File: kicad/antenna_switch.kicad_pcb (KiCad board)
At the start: 2 copper layers, 213.3 x 96 mm, 153 parts, among them J1 Conn_02x07_Odd_Even, J2 Conn_01x02, K1 Fujitsu_FTR-K1C, K10 Fujitsu_FTR-K1C, K11 Fujitsu_FTR-K1C, K12 Fujitsu_FTR-K1C, K13 Fujitsu_FTR-K1C, K14 Fujitsu_FTR-K1C, K15 Fujitsu_FTR-K1C, K16 Fujitsu_FTR-K1C, K17 Fujitsu_FTR-K1C, K18 Fujitsu_FTR-K1C, K2 Fujitsu_FTR-K1C, K3 Fujitsu_FTR-K1C, K4 Fujitsu_FTR-K1C, K5 Fujitsu_FTR-K1C, K6 Fujitsu_FTR-K1C, K7 Fujitsu_FTR-K1C, K8 Fujitsu_FTR-K1C, K9 Fujitsu_FTR-K1C, Q1 BC817, Q10 BC817, Q11 BC817, Q12 BC817, Q2 BC817, Q3 BC817, Q4 BC817, Q5 BC817, Q6 BC817, Q7 BC817, Q8 BC817, Q9 BC817

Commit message: reverse protection diode
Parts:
- added D45: ER1B, Diode_SMD:D_SMA_Handsoldering, F.Cu at (281.5, 99.7)
- moved F1 1.61 mm to (281.3, 92.4)
- moved D30 1.20 mm to (278.3, 93.0)
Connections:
- D30 pad 1: +12V -> Net-(D30-Pad1)
- F1 pad 2: +12V -> Net-(D30-Pad1)
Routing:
- net +12V: track 577.8 -> 567.8 mm
- net Net-(D30-Pad1): track 0.00 -> 6.48 mm
- net GND: track 194.5 -> 193.2 mm, vias 2795 -> 2366
- net Net-(F1-Pad1): track 5.81 -> 6.78 mm
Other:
- board text removed: "http://sq9nje.pl"

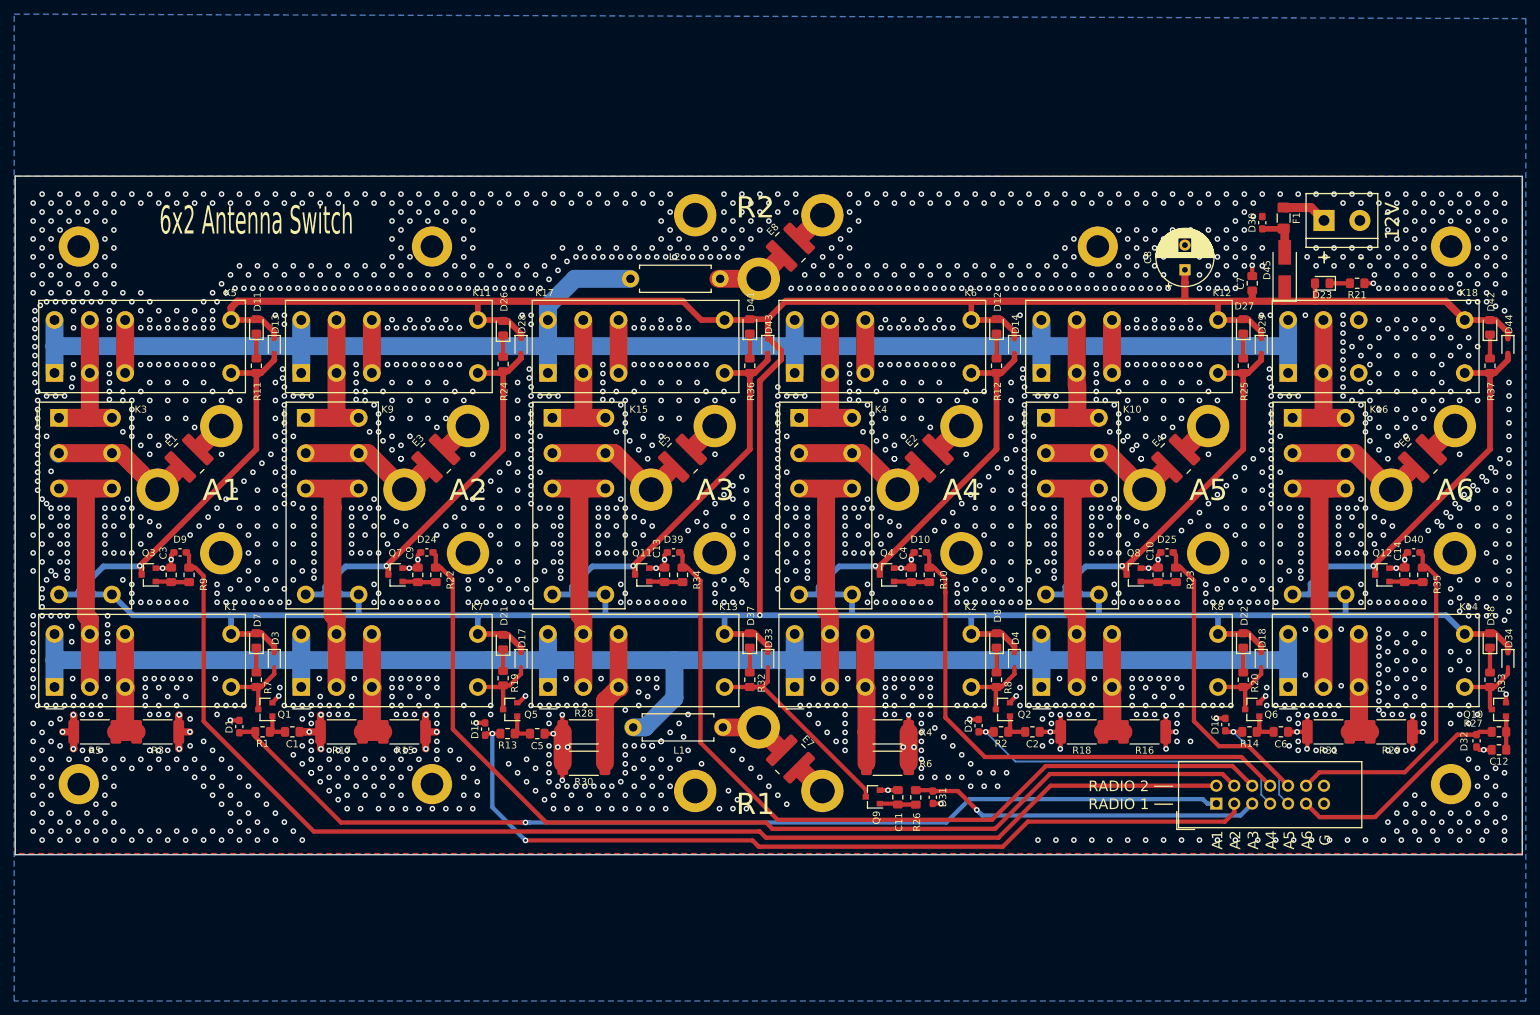
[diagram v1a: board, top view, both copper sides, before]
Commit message: less vias
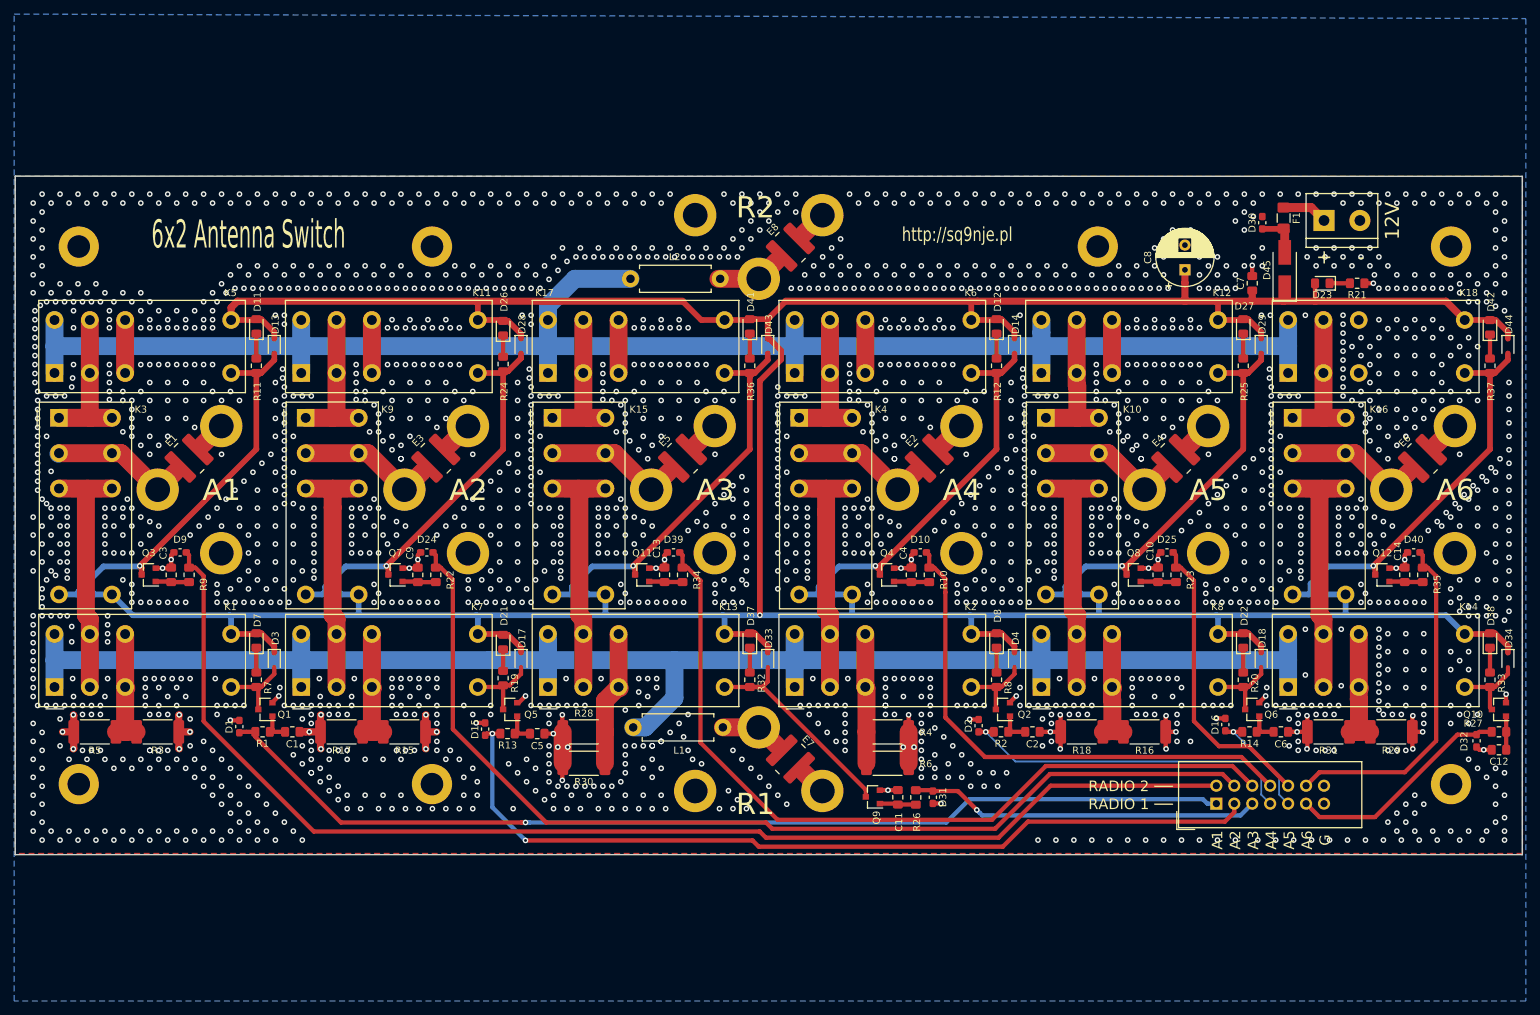
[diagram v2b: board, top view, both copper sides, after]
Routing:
- net GND: vias 2366 -> 2201
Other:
- board text added: "http://sq9nje.pl"

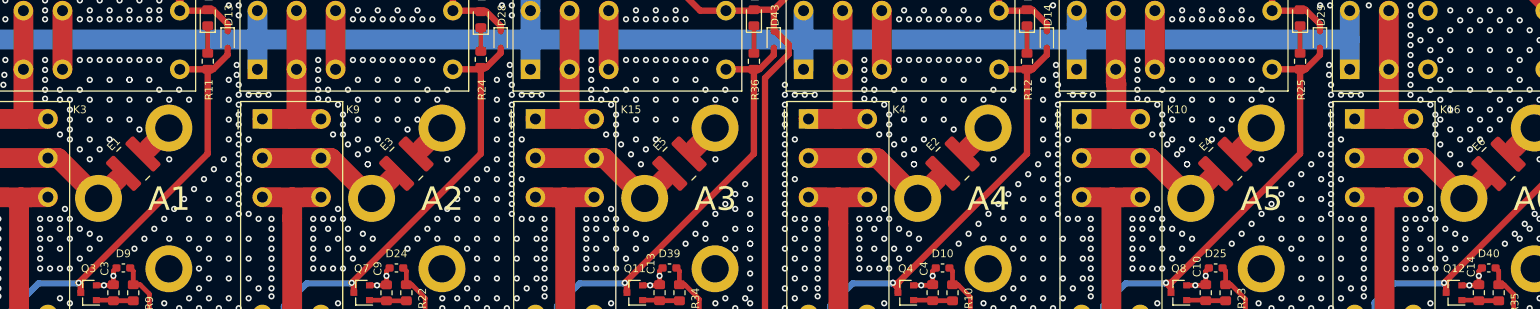
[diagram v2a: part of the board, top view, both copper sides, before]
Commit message: less vias
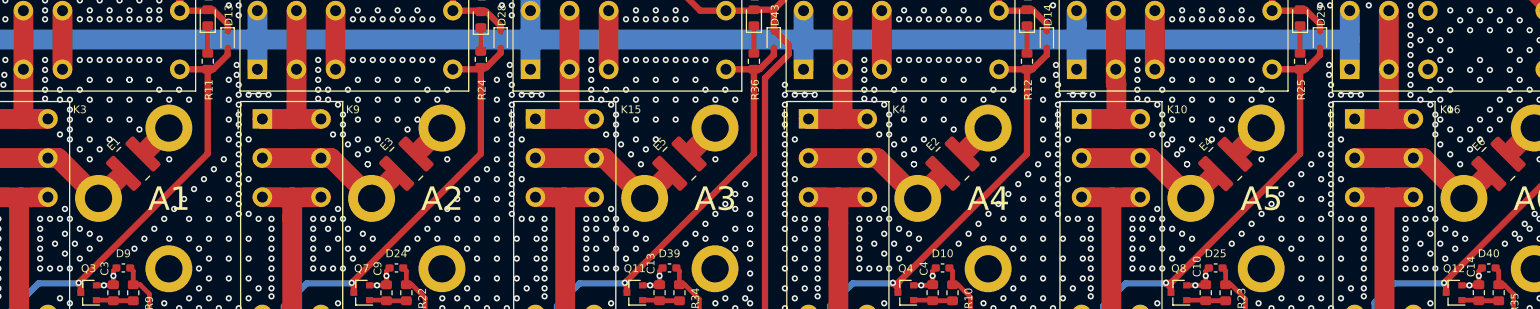
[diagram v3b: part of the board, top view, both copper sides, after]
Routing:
- net GND: vias 2201 -> 2196
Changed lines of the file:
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@@
     (thickness 1.6)
     (drawings 166)
-    (tracks 2976)
+    (tracks 2971)
     (zones 0)
     (modules 154)
@@
   (via (at 120.8024 123.2662) (size 0.8) (drill 0.4) (layers F.Cu B.Cu) (net 1))
   (via (at 122.0724 124.5362) (size 0.8) (drill 0.4) (layers F.Cu B.Cu) (net 1))
-  (via (at 116.9924 134.6962) (size 0.8) (drill 0.4) (layers F.Cu B.Cu) (net 1))
-  (via (at 118.2624 135.9662) (size 0.8) (drill 0.4) (layers F.Cu B.Cu) (net 1))
-  (via (at 115.7224 135.9662) (size 0.8) (drill 0.4) (layers F.Cu B.Cu) (net 1))
-  (via (at 116.9924 137.2362) (size 0.8) (drill 0.4) (layers F.Cu B.Cu) (net 1))
+  (via (at 117.6274 135.3312) (size 0.8) (drill 0.4) (layers F.Cu B.Cu) (net 1))
+  (via (at 118.8974 136.6012) (size 0.8) (drill 0.4) (layers F.Cu B.Cu) (net 1))
+  (via (at 116.3574 136.6012) (size 0.8) (drill 0.4) (layers F.Cu B.Cu) (net 1))
+  (via (at 117.6274 137.8712) (size 0.8) (drill 0.4) (layers F.Cu B.Cu) (net 1))
   (via (at 122.0724 158.8262) (size 0.8) (drill 0.4) (layers F.Cu B.Cu) (net 1))
   (via (at 124.6124 158.8262) (size 0.8) (drill 0.4) (layers F.Cu B.Cu) (net 1))
@@
   (via (at 210.9724 143.5862) (size 0.8) (drill 0.4) (layers F.Cu B.Cu) (net 1))
   (via (at 209.7024 144.8562) (size 0.8) (drill 0.4) (layers F.Cu B.Cu) (net 1))
-  (via (at 222.4024 135.9662) (size 0.8) (drill 0.4) (layers F.Cu B.Cu) (net 1))
-  (via (at 223.6724 137.2362) (size 0.8) (drill 0.4) (layers F.Cu B.Cu) (net 1))
-  (via (at 221.1324 137.2362) (size 0.8) (drill 0.4) (layers F.Cu B.Cu) (net 1))
-  (via (at 222.4024 138.5062) (size 0.8) (drill 0.4) (layers F.Cu B.Cu) (net 1))
+  (via (at 222.4024 135.3312) (size 0.8) (drill 0.4) (layers F.Cu B.Cu) (net 1))
+  (via (at 223.6724 136.6012) (size 0.8) (drill 0.4) (layers F.Cu B.Cu) (net 1))
+  (via (at 221.1324 136.6012) (size 0.8) (drill 0.4) (layers F.Cu B.Cu) (net 1))
+  (via (at 222.4024 137.8712) (size 0.8) (drill 0.4) (layers F.Cu B.Cu) (net 1))
   (via (at 236.3724 125.8062) (size 0.8) (drill 0.4) (layers F.Cu B.Cu) (net 1))
   (via (at 224.9424 115.6462) (size 0.8) (drill 0.4) (layers F.Cu B.Cu) (net 1))
@@
   (via (at 255.4224 137.2362) (size 0.8) (drill 0.4) (layers F.Cu B.Cu) (net 1))
   (via (at 257.9624 137.2362) (size 0.8) (drill 0.4) (layers F.Cu B.Cu) (net 1))
-  (via (at 290.9824 134.6962) (size 0.8) (drill 0.4) (layers F.Cu B.Cu) (net 1))
-  (via (at 292.2524 135.9662) (size 0.8) (drill 0.4) (layers F.Cu B.Cu) (net 1))
-  (via (at 290.9824 137.2362) (size 0.8) (drill 0.4) (layers F.Cu B.Cu) (net 1))
-  (via (at 293.5224 137.2362) (size 0.8) (drill 0.4) (layers F.Cu B.Cu) (net 1))
-  (via (at 292.2524 138.5062) (size 0.8) (drill 0.4) (layers F.Cu B.Cu) (net 1))
+  (via (at 292.2524 135.3312) (size 0.8) (drill 0.4) (layers F.Cu B.Cu) (net 1))
+  (via (at 290.9824 136.6012) (size 0.8) (drill 0.4) (layers F.Cu B.Cu) (net 1))
+  (via (at 293.5224 136.6012) (size 0.8) (drill 0.4) (layers F.Cu B.Cu) (net 1))
+  (via (at 292.2524 137.8712) (size 0.8) (drill 0.4) (layers F.Cu B.Cu) (net 1))
   (via (at 306.2224 125.8062) (size 0.8) (drill 0.4) (layers F.Cu B.Cu) (net 1))
   (via (at 270.6624 125.8062) (size 0.8) (drill 0.4) (layers F.Cu B.Cu) (net 1))
@@
   (via (at 304.9524 111.8362) (size 0.8) (drill 0.4) (layers F.Cu B.Cu) (net 1))
   (via (at 302.4124 111.8362) (size 0.8) (drill 0.4) (layers F.Cu B.Cu) (net 1))
-  (via (at 299.8724 111.8362) (size 0.8) (drill 0.4) (layers F.Cu B.Cu) (net 1))
-  (via (at 297.3324 111.8362) (size 0.8) (drill 0.4) (layers F.Cu B.Cu) (net 1))
   (via (at 294.7924 111.8362) (size 0.8) (drill 0.4) (layers F.Cu B.Cu) (net 1))
   (via (at 303.6824 113.1062) (size 0.8) (drill 0.4) (layers F.Cu B.Cu) (net 1))
@@
   (via (at 294.7924 116.9162) (size 0.8) (drill 0.4) (layers F.Cu B.Cu) (net 1))
   (via (at 292.2524 116.9162) (size 0.8) (drill 0.4) (layers F.Cu B.Cu) (net 1))
-  (via (at 297.3324 116.9162) (size 0.8) (drill 0.4) (layers F.Cu B.Cu) (net 1))
-  (via (at 299.8724 116.9162) (size 0.8) (drill 0.4) (layers F.Cu B.Cu) (net 1))
   (via (at 302.4124 116.9162) (size 0.8) (drill 0.4) (layers F.Cu B.Cu) (net 1))
   (via (at 304.9524 116.9162) (size 0.8) (drill 0.4) (layers F.Cu B.Cu) (net 1))
@@
   (via (at 293.5224 118.1862) (size 0.8) (drill 0.4) (layers F.Cu B.Cu) (net 1))
   (via (at 294.7924 119.4562) (size 0.8) (drill 0.4) (layers F.Cu B.Cu) (net 1))
-  (via (at 297.3324 119.4562) (size 0.8) (drill 0.4) (layers F.Cu B.Cu) (net 1))
   (via (at 299.8724 119.4562) (size 0.8) (drill 0.4) (layers F.Cu B.Cu) (net 1))
   (via (at 302.4124 119.4562) (size 0.8) (drill 0.4) (layers F.Cu B.Cu) (net 1))
@@
   (via (at 292.2524 111.8362) (size 0.8) (drill 0.4) (layers F.Cu B.Cu) (net 1))
   (via (at 151.2824 134.6962) (size 0.8) (drill 0.4) (layers F.Cu B.Cu) (net 1))
-  (via (at 221.1324 134.6962) (size 0.8) (drill 0.4) (layers F.Cu B.Cu) (net 1))
   (via (at 242.7224 135.9662) (size 0.8) (drill 0.4) (layers F.Cu B.Cu) (net 1))
   (via (at 240.1824 138.5062) (size 0.8) (drill 0.4) (layers F.Cu B.Cu) (net 1))
@@
   (via (at 191.9224 168.9862) (size 0.8) (drill 0.4) (layers F.Cu B.Cu) (net 1))
   (via (at 190.6524 170.2562) (size 0.8) (drill 0.4) (layers F.Cu B.Cu) (net 1))
+  (via (at 298.6024 115.6462) (size 0.8) (drill 0.4) (layers F.Cu B.Cu) (net 1))
+  (via (at 298.6024 113.1062) (size 0.8) (drill 0.4) (layers F.Cu B.Cu) (net 1))
   (segment (start 107.87 125.73) (end 107.95 125.65) (width 2.54) (layer B.Cu) (net 2))
   (segment (start 107.95 125.65) (end 115.45 125.65) (width 2.54) (layer F.Cu) (net 2))
